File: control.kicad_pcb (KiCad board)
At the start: 4 copper layers, 151.6 x 109.5 mm, 174 parts, among them J1 Wurth_THR_Terminal_M4, J10 Conn_02x20_Odd_Even, J11 Conn_ARM_JTAG_SWD_10, J12 TE_Faston_20-16AWG_Straight_T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, J13 TE_Faston_20-16AWG_Straight_T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, J14 TE_Faston_20-16AWG_Straight_T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, J15 TE_Faston_20-16AWG_Straight_T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, J16 TE_Faston_20-16AWG_Straight_T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, J17 TE_Faston_20-16AWG_Straight_T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, J18 TE_Faston_20-16AWG_Straight_T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, J19 TE_Faston_20-16AWG_Straight_T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, J2 Wurth_THR_Terminal_M4, J20 TE_Faston_20-16AWG_Straight_T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, J21 TE_Faston_20-16AWG_Straight_T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, J22 TE_Faston_20-16AWG_Straight_T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, J23 TE_Faston_20-16AWG_Straight_T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, J24 TE_Faston_20-16AWG_Straight_T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, J25 TE_Faston_20-16AWG_Straight_T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, J26 TE_Faston_20-16AWG_Straight_T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, J27 TE_Faston_20-16AWG_Straight_T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, J3 Conn_02x08_Odd_Even, J4 Conn_02x08_Odd_Even, J5 Conn_02x08_Odd_Even, J6 Conn_02x08_Odd_Even, J7 Conn_02x08_Odd_Even, J8 TE_Faston_20-16AWG_Straight_T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, J9 TE_Faston_20-16AWG_Straight_T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, SW1 SW_Push, U1 TPS7B8733, U2 MAX33071, U3 ATSAMD21J18A-A, U4 TCMT4600, U5 TCMT4600, U6 TCMT4600, U7 TCMT4600, U8 TCMT4600, U9 TCMT4600, Y1 32.768kHz

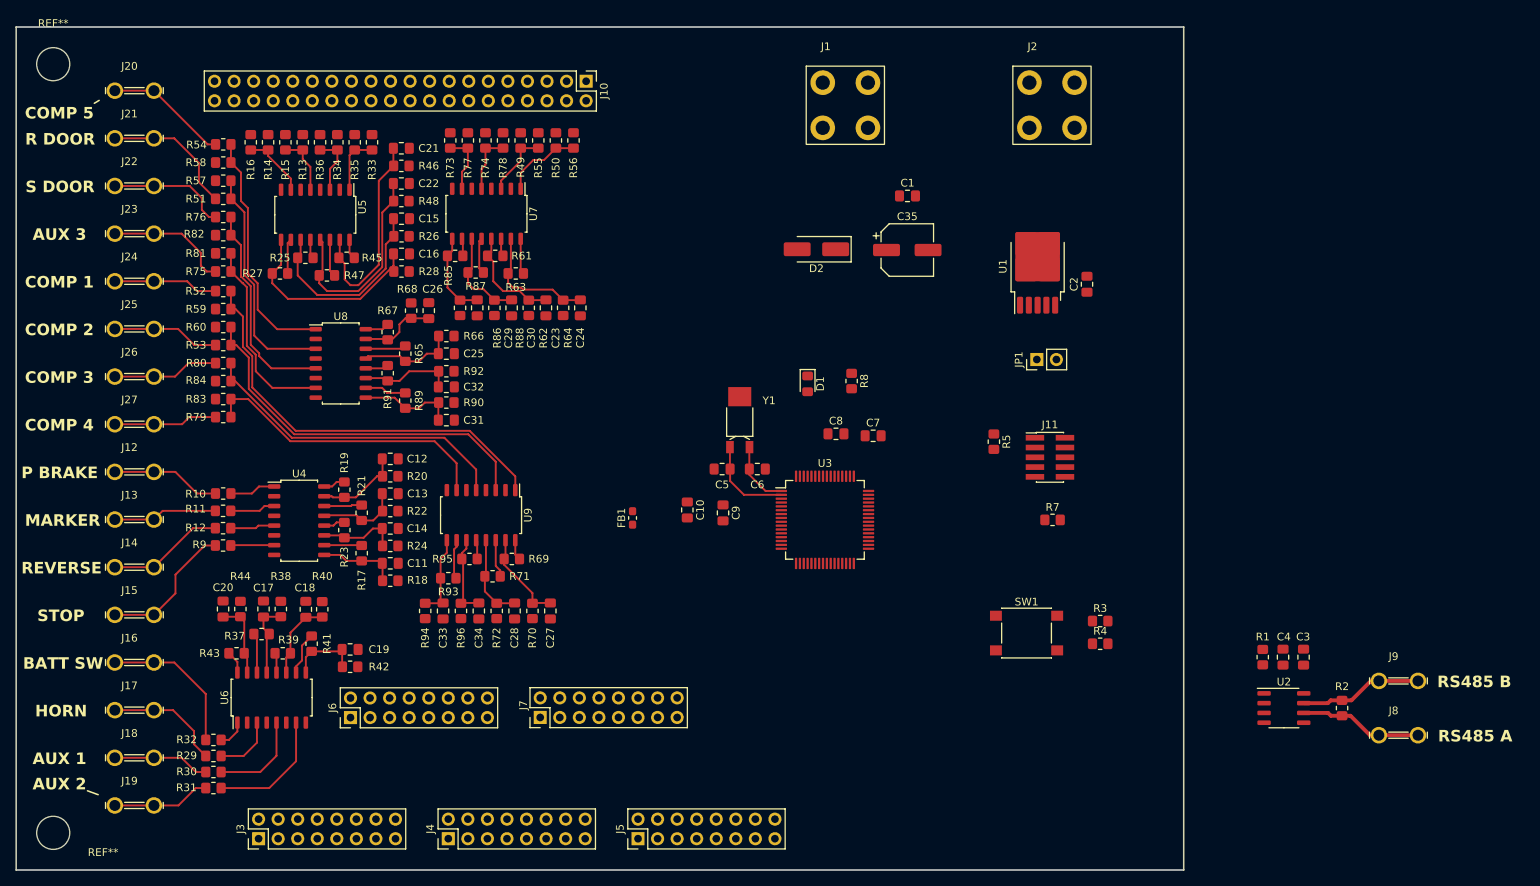
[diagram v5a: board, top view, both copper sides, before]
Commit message: lay pre-autorouting tracks
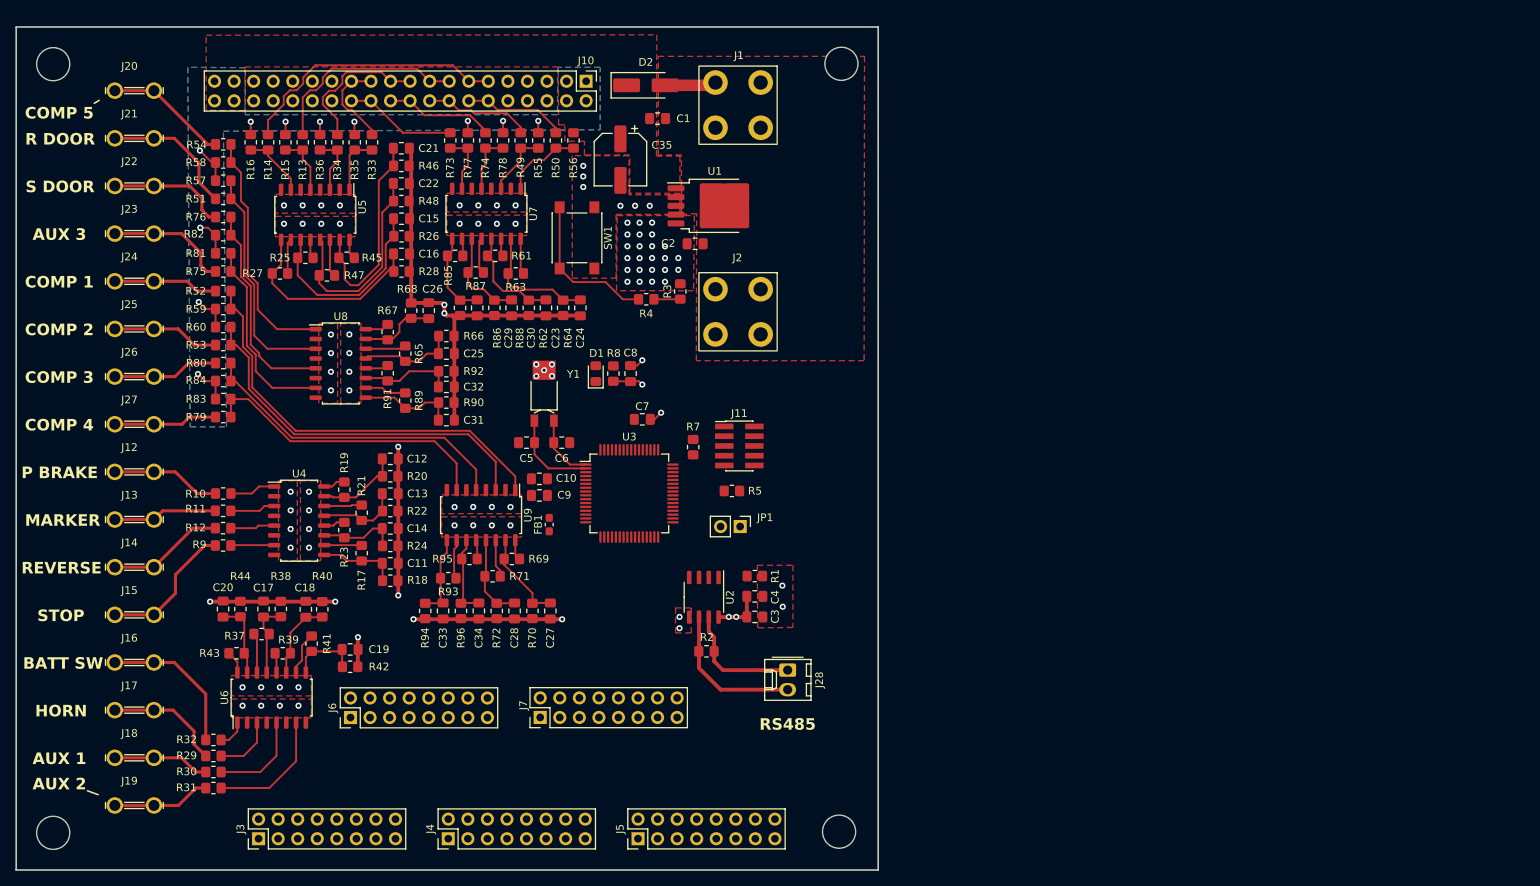
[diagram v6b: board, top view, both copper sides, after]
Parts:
- removed J8, J9: TE_Faston_20-16AWG_Straight_Tab, Toadly:TE_Faston_20-16AWG_Straight_Tab
- added J28: Conn_01x02, Connector_Molex:Molex_KK-254_AE-6410-02A_1x02_P2.54mm_Vertical, F.Cu at (171.1, 125.9)
- added MH2: MountingHole_4.3mm_M4, MountingHole:MountingHole_4.3mm_M4, F.Cu at (178.1, 47.2)
- added MH4: MountingHole_4.3mm_M4, MountingHole:MountingHole_4.3mm_M4, F.Cu at (177.7, 146.9)
- moved R2 82.9 mm to (160.5, 123.5), turned to 0 degrees
- moved SW1 77.7 mm to (143.7, 69.8), turned to -90 degrees
- moved U2 76.7 mm to (160.2, 116.5), turned to -90 degrees
- moved R4 74.0 mm to (152.7, 77.8)
- moved C3 71.5 mm to (166.8, 119.0), turned to 0 degrees
- moved R3 69.3 mm to (157.1, 76.8), turned to 90 degrees
- moved C4 69.0 mm to (166.8, 116.4), turned to 0 degrees
- moved R1 66.8 mm to (166.8, 113.7), turned to 0 degrees
- moved C2 51.2 mm to (159.1, 70.6), turned to 0 degrees
- moved J2 48.8 mm to (164.6, 79.4), turned to -90 degrees
- moved R7 47.6 mm to (158.8, 97.0), turned to 90 degrees
- moved JP1 44.2 mm to (164.9, 107.3), turned to -90 degrees
- moved U1 42.7 mm to (161.6, 65.6), turned to 0 degrees
- moved J11 40.4 mm to (164.8, 96.8)
- moved C35 39.1 mm to (149.4, 59.6), turned to -90 degrees
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- renumbered REF** to MH1, REF** to MH3
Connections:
- J4 pad 6: CAB_CHIME_EN -> MARKER_LGT_EN
- U3 pad 10: COMP_5_LGT_EN -> CAB_1_SENSE
- U3 pad 11: COMP_1_SENSE -> CAB_2_SENSE
- U3 pad 12: COMP_2_SENSE -> CAB_3_SENSE
- U3 pad 13: FOG_LGT_EN -> FLOOD_D_EN
- U3 pad 14: ISECT_D_EN -> FLOOD_R_EN
- U3 pad 15: ISECT_P_EN -> FLOOD_P_EN
- U3 pad 17: PARK_BRAKE_SENSE -> AUX_2_EN
- U3 pad 18: MARKER_LIGHT_SENSE -> AUX_3_EN
- U3 pad 19: STOP_LIGHT_SENSE -> MARKER_LGT_EN
- U3 pad 20: REVERSE_LIGHT_SENSE -> BACKUP_CHIME_EN
- U3 pad 23: COMP_3_SENSE -> FOG_LGT_EN
- U3 pad 24: COMP_4_SENSE -> ISECT_D_EN
- U3 pad 25: COMP_5_SENSE -> ISECT_P_EN
- U3 pad 26: CAB_1_SENSE -> AUX_4_EN
- U3 pad 27: CAB_2_SENSE -> AUX_5_EN
- U3 pad 28: CAB_3_SENSE -> COMP_1_LGT_EN
- U3 pad 29: HORN_SENSE -> COMP_2_LGT_EN
- U3 pad 3: CAB_CHIME_EN -> BATT_SW_SENSE
- U3 pad 30: SIDE_DOOR_SENSE -> COMP_3_LGT_EN
- U3 pad 31: REAR_DOOR_SENSE -> COMP_4_LGT_EN
- U3 pad 32: BATT_SW_SENSE -> COMP_5_LGT_EN
- U3 pad 35: AUX_1_SENSE -> RS485_DATA_ENABLE
- U3 pad 36: AUX_2_SENSE -> PARK_BRAKE_SENSE
- U3 pad 37: AUX_3_SENSE -> MARKER_LIGHT_SENSE
- U3 pad 38: CAB_6_SENSE -> STOP_LIGHT_SENSE
- U3 pad 4: BACKUP_CHIME_EN -> HORN_SENSE
- U3 pad 41: CAB_7_SENSE -> REVERSE_LIGHT_SENSE
- U3 pad 42: CAB_8_SENSE -> SIDE_DOOR_SENSE
- U3 pad 45: RS485_DATA_ENABLE -> CAB_7_SENSE
- U3 pad 46: AUX_2_EN -> CAB_8_SENSE
- U3 pad 5: COMP_2_LGT_EN -> AUX_1_SENSE
- U3 pad 51: AUX_3_EN -> AUX_3_SENSE
- U3 pad 53: AUX_4_EN -> CAB_6_SENSE
- U3 pad 6: COMP_3_LGT_EN -> AUX_2_SENSE
- U3 pad 60: AUX_5_EN -> REAR_DOOR_SENSE
- U3 pad 61: FLOOD_D_EN -> COMP_1_SENSE
- U3 pad 62: FLOOD_R_EN -> COMP_2_SENSE
- U3 pad 63: FLOOD_P_EN -> COMP_3_SENSE
- U3 pad 64: COMP_1_LGT_EN -> COMP_4_SENSE
- U3 pad 9: COMP_4_LGT_EN -> COMP_5_SENSE
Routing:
- net GNDREF: track 0.00 -> 119.5 mm, vias 0 -> 50
- net FLOOD_P_EN: track 0.00 -> 67.5 mm
- net COMP_1_LGT_EN: track 0.00 -> 55.1 mm
- net AUX_2_EN: track 0.00 -> 48.0 mm
- net BACKUP_CHIME_EN: track 0.00 -> 47.8 mm
- net ISECT_D_EN: track 0.00 -> 39.7 mm
- net COMP_5_SENSE: track 9.99 -> 48.3 mm
- net CAB_SIGNAL_1: track 0.00 -> 35.4 mm
- net PARK_BRAKE_SENSE: track 11.0 -> 44.1 mm
- net +12V: track 0.00 -> 31.0 mm, vias 0 -> 11
- net AUX_5_EN: track 0.00 -> 27.8 mm
- net CAB_SIGNAL_2: track 0.00 -> 26.5 mm
- net Net-(D2-A): track 0.00 -> 24.3 mm
- net REAR_DOOR_SENSE: track 12.5 -> 36.6 mm
- net Net-(R4-Pad1): track 0.00 -> 19.8 mm
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- added copper zone on B.Cu, net +12V
- added copper zone on F.Cu, net +12V
- added copper zone on F.Cu, net +3.3V
- added copper zone on In2.Cu, net +3.3V
- added copper zone on F.Cu, net GNDREF
- added copper zone on In1.Cu, net GNDREF
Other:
- board size 151.6 x 109.5 mm -> 111.9 x 109.5 mm
- board text added: "RS485"
- board text removed: "RS485 A"
- board text removed: "RS485 B"

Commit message: route all tracks
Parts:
- moved R7 9.41 mm to (164.9, 89.8), turned to 180 degrees
- moved FB1 0.89 mm to (140.3, 106.2), turned to -90 degrees
- moved R2 0.86 mm to (161.4, 123.5)
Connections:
- J10 pad 10: /RS485_B -> /RS485_A
- J10 pad 9: /RS485_A -> /RS485_B
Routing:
- net /RS485_B: track 16.1 -> 118.8 mm, vias 0 -> 1
- net /RS485_A: track 19.3 -> 119.2 mm, vias 0 -> 1
- net CAB_4_SENSE: track 27.3 -> 101.4 mm, vias 0 -> 4
- net FLOOD_D_EN: track 2.54 -> 69.8 mm
- net CAB_1_SENSE: track 26.0 -> 91.2 mm, vias 0 -> 5
- net HORN_SENSE: track 9.93 -> 73.6 mm, vias 0 -> 2
- net FLOOD_R_EN: track 2.54 -> 66.0 mm
- net BATT_SW_SENSE: track 9.88 -> 73.1 mm, vias 0 -> 2
- net SIDE_DOOR_SENSE: track 12.2 -> 73.2 mm, vias 0 -> 4
- net CAB_2_SENSE: track 25.6 -> 84.6 mm, vias 0 -> 3
- net AUX_1_SENSE: track 10.4 -> 67.5 mm, vias 0 -> 2
- net CAB_3_SENSE: track 27.3 -> 82.5 mm, vias 0 -> 3
- net ISECT_P_EN: track 0.00 -> 52.7 mm
- net AUX_2_SENSE: track 9.39 -> 61.8 mm, vias 0 -> 2
- net STOP_LIGHT_SENSE: track 10.3 -> 61.7 mm, vias 0 -> 2
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
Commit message: fix DRC errors
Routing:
- net Net-(J11-~{RESET}): track 15.1 -> 11.7 mm
- net GNDREF: track 147.5 -> 149.4 mm
- net PARK_BRAKE_SENSE: track 56.0 -> 57.2 mm
- net Net-(U3-PA01): track 11.8 -> 10.9 mm
